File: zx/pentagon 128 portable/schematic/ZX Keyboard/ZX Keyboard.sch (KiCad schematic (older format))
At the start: 48 parts, among them IC1 SN74LS245DW, IC2 SN74LS27N, IC3 SN74LS245DW

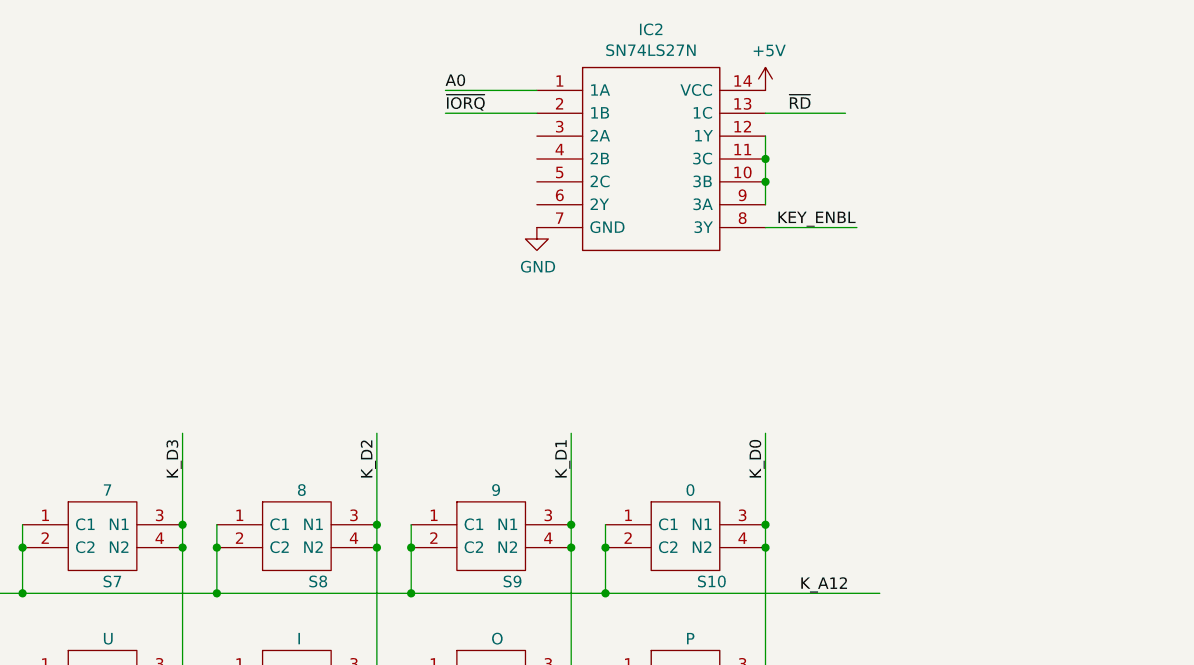
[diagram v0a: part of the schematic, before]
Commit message: reorganizing. finished ram and keyboard, updated z80
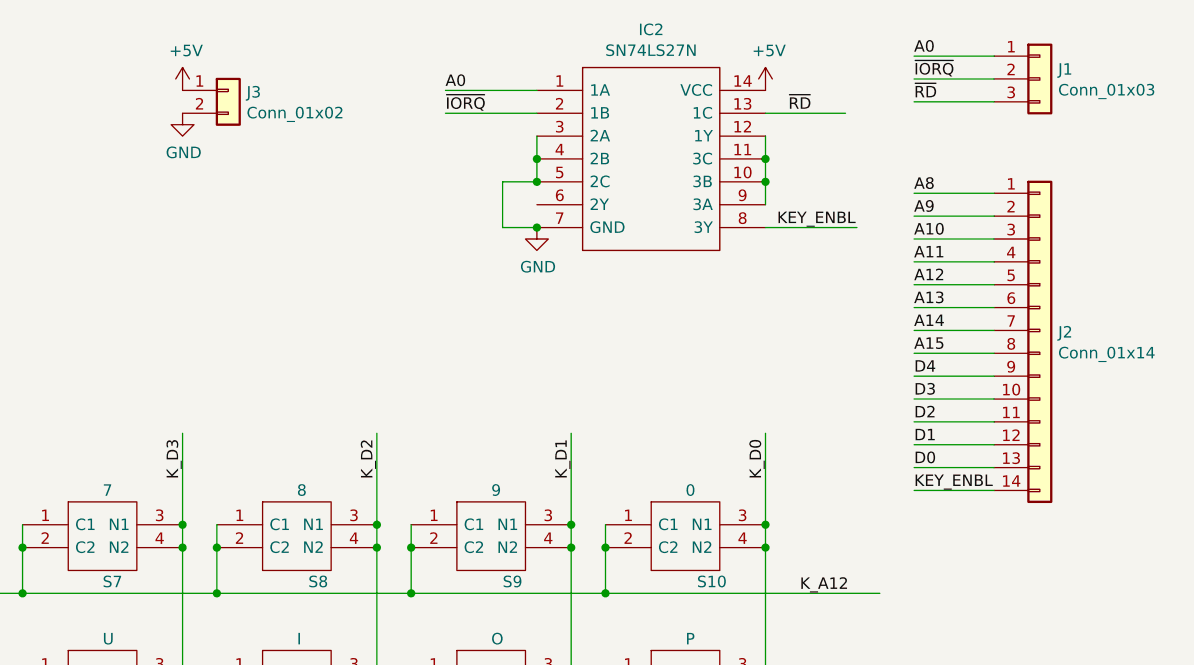
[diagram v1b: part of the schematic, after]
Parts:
- added J1: Conn_01x03, Connector_PinHeader_2.54mm:PinHeader_1x03_P2.54mm_Vertical, symbol Connector_Generic:Conn_01x03
- added J2: Conn_01x14, Connector_PinHeader_2.54mm:PinHeader_1x14_P2.54mm_Vertical, symbol Connector_Generic:Conn_01x14
- added J3: Conn_01x02, Connector_PinHeader_2.54mm:PinHeader_1x02_P2.54mm_Vertical, symbol Connector_Generic:Conn_01x02
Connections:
- wire segments 244 -> 266
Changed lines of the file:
@@
 Text Label 9800 1550 0    50   ~ 0
 KEY_ENBL
+$Comp
+L Connector_Generic:Conn_01x03 J1
+U 1 1 5F648B45
+P 10950 900
+F 0 "J1" H 11030 942 50  0000 L CNN
+F 1 "Conn_01x03" H 11030 851 50  0000 L CNN
+F 2 "Connector_PinHeader_2.54mm:PinHeader_1x03_P2.54mm_Vertical" H 10950 900 50  0001 C CNN
+F 3 "~" H 10950 900 50  0001 C CNN
+	1    10950 900
+	1    0    0    -1
+$EndComp
+Wire Wire Line
+	10750 800  10400 800
+Wire Wire Line
+	10750 900  10400 900
+Wire Wire Line
+	10750 1000 10400 1000
+Text Label 10400 800  0    50   ~ 0
+A0
+Text Label 10400 1000 0    50   ~ 0
+~RD
+Text Label 10400 900  0    50   ~ 0
+~IORQ
+$Comp
+L Connector_Generic:Conn_01x14 J2
+U 1 1 5F68D465
+P 10950 2000
+F 0 "J2" H 11030 1992 50  0000 L CNN
+F 1 "Conn_01x14" H 11030 1901 50  0000 L CNN
+F 2 "Connector_PinHeader_2.54mm:PinHeader_1x14_P2.54mm_Vertical" H 10950 2000 50  0001 C CNN
+F 3 "~" H 10950 2000 50  0001 C CNN
+	1    10950 2000
+	1    0    0    -1
+$EndComp
+Wire Wire Line
+	10750 1400 10400 1400
+Wire Wire Line
+	10750 1500 10400 1500
+Wire Wire Line
+	10750 1600 10400 1600
+Wire Wire Line
+	10750 1700 10400 1700
+Wire Wire Line
+	10750 1800 10400 1800
+Wire Wire Line
+	10750 1900 10400 1900
+Wire Wire Line
+	10750 2000 10400 2000
+Wire Wire Line
+	10750 2100 10400 2100
+Wire Wire Line
+	10750 2200 10400 2200
+Wire Wire Line
+	10750 2300 10400 2300
+Wire Wire Line
+	10750 2400 10400 2400
+Wire Wire Line
+	10750 2500 10400 2500
+Wire Wire Line
+	10750 2600 10400 2600
+Wire Wire Line
+	10750 2700 10400 2700
+Text Label 10400 2700 0    50   ~ 0
+KEY_ENBL
+Text Label 10400 1400 0    50   ~ 0
+A8
+Text Label 10400 1500 0    50   ~ 0
+A9
+Text Label 10400 1600 0    50   ~ 0
+A10
+Text Label 10400 1700 0    50   ~ 0
+A11
+Text Label 10400 1800 0    50   ~ 0
+A12
+Text Label 10400 1900 0    50   ~ 0
+A13
+Text Label 10400 2000 0    50   ~ 0
+A14
+Text Label 10400 2100 0    50   ~ 0
+A15
+Text Label 10400 2600 0    50   ~ 0
+D0
+Text Label 10400 2500 0    50   ~ 0
+D1
+Text Label 10400 2400 0    50   ~ 0
+D2
+Text Label 10400 2300 0    50   ~ 0
+D3
+Text Label 10400 2200 0    50   ~ 0
+D4
+$Comp
+L Connector_Generic:Conn_01x02 J3
+U 1 1 5F885BE0
+P 7400 950
+F 0 "J3" H 7480 942 50  0000 L CNN
+F 1 "Conn_01x02" H 7480 851 50  0000 L CNN
+F 2 "Connector_PinHeader_2.54mm:PinHeader_1x02_P2.54mm_Vertical" H 7400 950 50  0001 C CNN
+F 3 "~" H 7400 950 50  0001 C CNN
+	1    7400 950
+	1    0    0    -1
+$EndComp
+$Comp
+L power:+5V #PWR0109
+U 1 1 5F8866E2
+P 7200 950
+F 0 "#PWR0109" H 7200 800 50  0001 C CNN
+F 1 "+5V" H 7215 1123 50  0000 C CNN
+F 2 "" H 7200 950 50  0001 C CNN
+F 3 "" H 7200 950 50  0001 C CNN
+	1    7200 950
+	1    0    0    -1
+$EndComp
+$Comp
+L power:GND #PWR0110
+U 1 1 5F886BFC
+P 7200 1050
+F 0 "#PWR0110" H 7200 800 50  0001 C CNN
+F 1 "GND" H 7205 877 50  0000 C CNN
+F 2 "" H 7200 1050 50  0001 C CNN
+F 3 "" H 7200 1050 50  0001 C CNN
+	1    7200 1050
+	1    0    0    -1
+$EndComp
+Wire Wire Line
+	8750 1150 8750 1250
+Wire Wire Line
+	8750 1250 8750 1350
+Connection ~ 8750 1250
+Wire Wire Line
+	8750 1350 8600 1350
+Wire Wire Line
+	8600 1350 8600 1550
+Wire Wire Line
+	8600 1550 8750 1550
+Connection ~ 8750 1350
+Connection ~ 8750 1550
 $EndSCHEMATC
